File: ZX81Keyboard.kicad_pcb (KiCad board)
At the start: 2 copper layers, 153 x 58 mm, 53 parts, among them J2 Conn_01x05, J3 Conn_01x03, J4 Conn_01x08, SW1 1, SW10 0, SW11 Q, SW12 W, SW13 E, SW14 R, SW15 T, SW16 Y, SW17 U, SW18 I, SW19 O, SW2 2, SW20 P, SW21 A, SW22 S, SW23 D, SW24 F, SW25 G, SW26 H, SW27 J, SW28 K, SW29 L, SW3 3, SW30 NEW_LINE, SW31 SHIFT, SW32 Z, SW33 X, SW34 C, SW35 V, SW36 B, SW37 N, SW38 M, SW39 ., SW4 4, SW40 SPACE, SW5 5, SW6 6, SW7 7, SW8 8, SW9 9

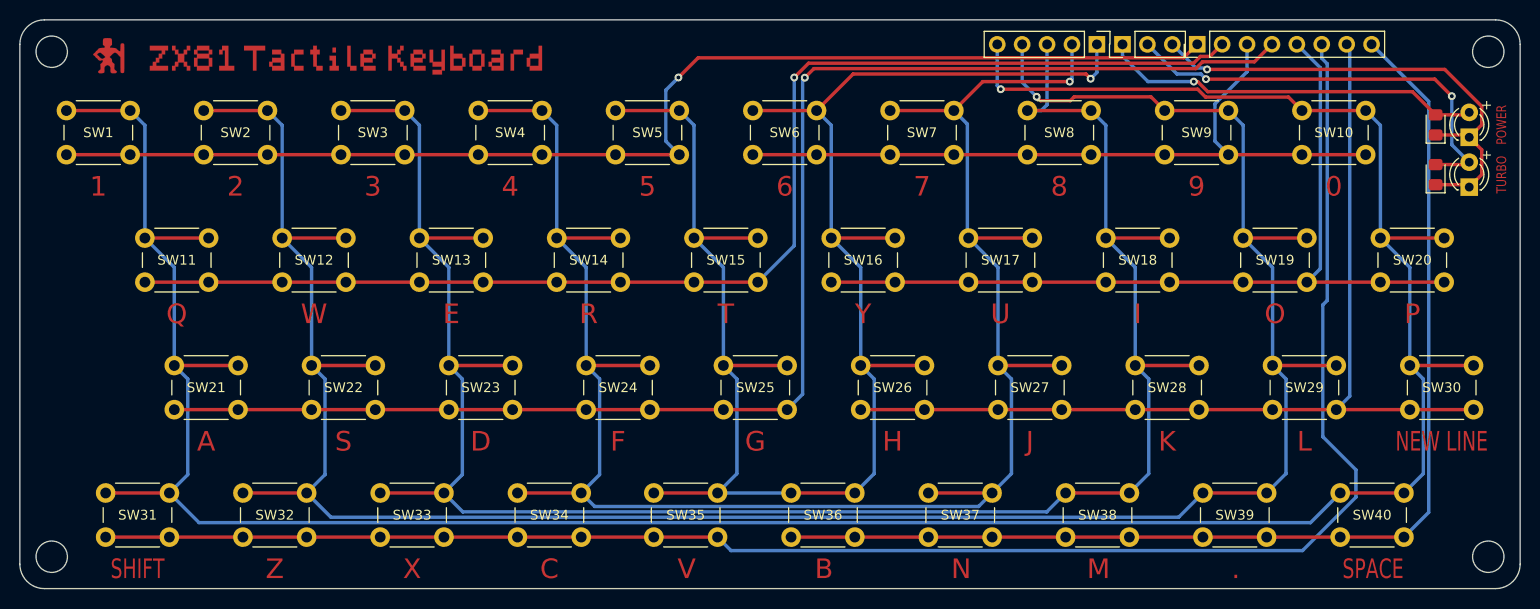
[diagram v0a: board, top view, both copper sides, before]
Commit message: Converted to KiCAD 7 file formats.
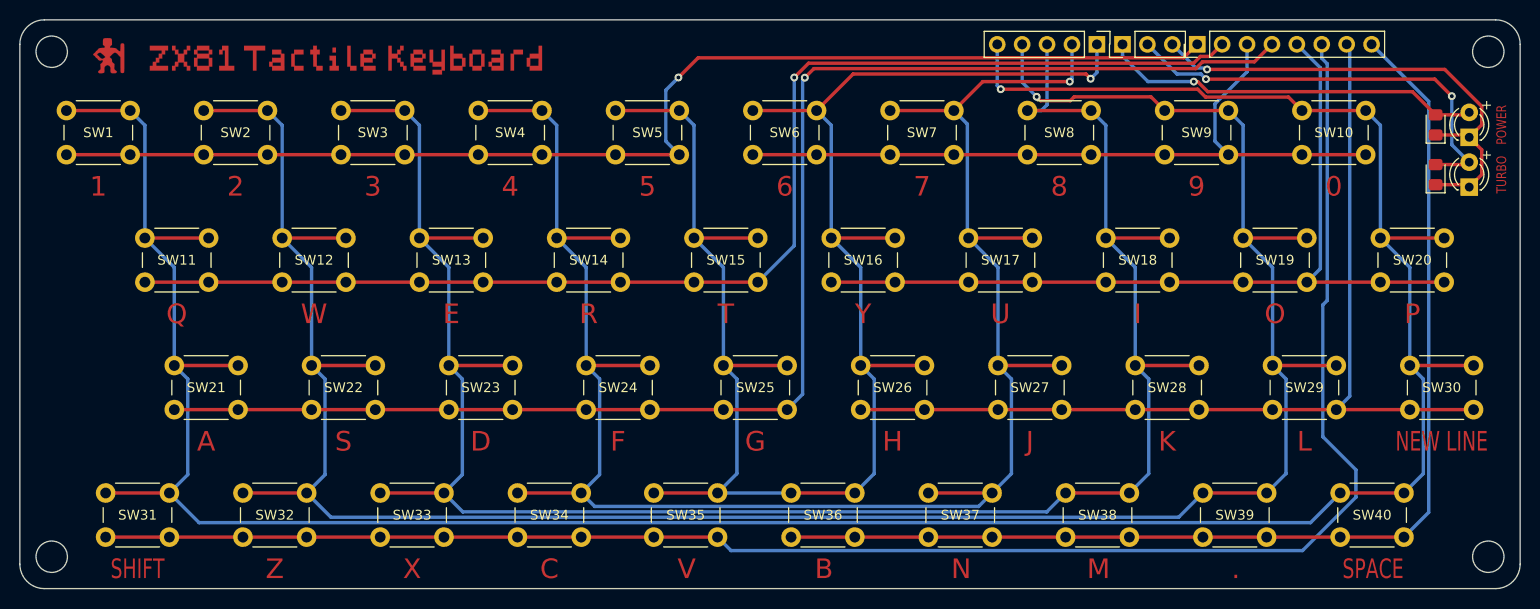
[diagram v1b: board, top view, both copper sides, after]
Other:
- net class Default removed

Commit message: Rotated connector back again to better accommodate rev. 1.9 of the motherboard.
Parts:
- moved J2 10.1 mm to (162.0, 68.2), turned to 90 degrees
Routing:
- net KD4: track 177.5 -> 166.6 mm
- net KD0: track 294.7 -> 283.9 mm
- net KD3: track 196.4 -> 190.0 mm, vias 1 -> 0
- net KD1: track 249.8 -> 244.5 mm
- net KD2: track 209.9 -> 209.1 mm
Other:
- board text added: "KD0 KD1 KD2 KD3 KD4"
- board text added: "ZX81 Tactile Keyboard Rev.3"
- board text removed: "KD4 KD3 KD2 KD1 KD0"
- board text removed: "ZX81 Tactile Keyboard Rev.2"
